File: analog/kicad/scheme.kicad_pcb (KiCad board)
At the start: 2 copper layers, 58 x 24 mm, 17 parts, among them J1 Barrel_Jack_Switch, U1 LM324

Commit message: pcb
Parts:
- added R10: 10k, Resistor_SMD:R_0603_1608Metric, F.Cu at (132.2, 92.0)
- added R11: 12.5k, Resistor_SMD:R_0603_1608Metric, F.Cu at (132.2, 94.5)
- moved R3 3.57 mm to (133.0, 86.0)
- moved R5 0.50 mm to (150.8, 102.0)
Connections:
- net BIAS renamed /BIAS
- J1 pad 1: Net-(U1E-V+) -> Net-(J1-Pad1)
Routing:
- net /BIAS: track 22.5 -> 18.6 mm
- net Net-(J1-Pad1): track 0.00 -> 3.00 mm
- net Net-(U1E-V+): track 49.5 -> 48.2 mm
- net /dist2: track 12.5 -> 11.8 mm

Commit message: changes to pcb
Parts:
- removed the R10 at (132.2, 92.0)
- removed the R11 at (132.2, 94.5)
- added C3: 10u, Capacitor_SMD:C_0805_2012Metric, F.Cu at (128.0, 93.5)
- added C4: 10u, Capacitor_SMD:C_0805_2012Metric, F.Cu at (137.5, 100.5)
- added R7: 1.6k, Resistor_SMD:R_0805_2012Metric, F.Cu at (131.4, 95.0)
- added R8: 4.7k, Resistor_SMD:R_0805_2012Metric, F.Cu at (131.4, 90.8)
- added U2: LM7805_TO220, Package_TO_SOT_THT:TO-220-3_Vertical, F.Cu at (128.4, 101.0)
- C1, C2: footprint Capacitor_SMD:C_0603_1608Metric -> Capacitor_SMD:C_0805_2012Metric
- R1: renamed from R2; footprint Resistor_SMD:R_0603_1608Metric -> Resistor_SMD:R_0805_2012Metric
- R10: renamed from R8; footprint Resistor_SMD:R_0603_1608Metric -> Resistor_SMD:R_0805_2012Metric
- R11: renamed from R9; footprint Resistor_SMD:R_0603_1608Metric -> Resistor_SMD:R_0805_2012Metric
- R2: renamed from R1; footprint Resistor_SMD:R_0603_1608Metric -> Resistor_SMD:R_0805_2012Metric
- R3, R4, R5, R6: footprint Resistor_SMD:R_0603_1608Metric -> Resistor_SMD:R_0805_2012Metric
- R9: renamed from R7; footprint Resistor_SMD:R_0603_1608Metric -> Resistor_SMD:R_0805_2012Metric
- moved J1 4.00 mm to (124.3, 92.0)
- moved R2 0.90 mm to (137.4, 95.2)
- moved R5 0.51 mm to (150.8, 102.5)
- moved C1 0.50 mm to (140.0, 95.3)
- moved R6 0.50 mm to (158.0, 102.5)
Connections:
- net Net-(U1E-V+) renamed +5V
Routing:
- net +5V: track 48.2 -> 72.7 mm
- net Net-(U2-GND): track 0.00 -> 10.4 mm
- net Net-(U2-VI): track 3.00 -> 11.5 mm
- net /BIAS: track 18.6 -> 17.0 mm
- net /OUT: track 30.0 -> 29.2 mm
- net Net-(D1-A): track 16.7 -> 16.1 mm
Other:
- board size 58 x 24 mm -> 62.5 x 27 mm

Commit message: comments and schematic update
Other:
- board text added: "Peale vaadates on trükkplaat üsna kena, aga mõned asjad jäid silma 1) Komponentide nimed R5, R6 ja D4 on kindlasti liiga trükkplaadi ääre lähedal 2) Mõelge kindlasti, kas saate 0603 komponentide jootmisega hakkama 3) Hetkel on trükkplaadi rajad 0.2 mm ehk ac 8 milsi laiad. ise soovitan rajad teha kindlasti 10/10 reeglite järgi, kusjuures toite rajad soovitan teha isegi laiemad, kuni 40 mils. Kuna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"
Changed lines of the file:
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@@
 		(layer "Edge.Cuts")
+	)
+	(gr_text "Peale vaadates on trükkplaat üsna kena, aga mõned asjad jäid silma\n1) Komponentide nimed R5, R6 ja D4 on kindlasti liiga trükkplaadi ääre lähedal\n2) Mõelge kindlasti, kas saate 0603 komponentide jootmisega hakkama\n3) Hetkel on trükkplaadi rajad 0.2 mm ehk ac 8 milsi laiad. ise soovitan rajad teha kindlasti 10/10\nreeglite järgi, kusjuures toite rajad soovitan teha isegi laiemad, kuni 40 mils. \nKuna plaadil ruumi on, siis ega paha ei tee, kui ka muud rajad on laiemad\n4) lisage nn Power good LED (ehk toitesse üks, mis lihtaslt indikeerib, kas toide on olemas või ei)\n5) Soovitan mõelda, et kas trükkplaat läheb ka kusagile korpusesse ja siis teha \ntrükkplaadi väliskuju korpuse järgi\n6) Viade suurus on hetkel 03/06, soovitan vähemalt 05/08 suurust\n7) Võite kaaluda ka valgusdioodide SMD vastu vahetamisele (aga see on teie otsus).\nKui seade läheb nt korpusesse, ehk ongi THT komponent parem).\n8) U1 on ka kindlasti SMD-na saadaval. Kaaluge, kas selle kasutamine võiks anda mingisuguseid eeliseid\n9) Skeemis vististi mainisin, aga U1 tahab kindlasti toitekondensaatorit ning sisend tahab kaitsmist\n10) Paigutuse mõistes mõelge sellele, et kuivõrd D2-D4 võivad hakata mõjutama mõõtetulemusi. Ehk on kasulikum D2-D4\npaigutada nii, et nad saab plaadiga tasapinda panna (hetkel 90 kraadise nurga all)\n11) Ehk on toite osas mõistlik mõelda mingisuguse patarei lahenduse peale (+ siis sisse/väljalülitamiseks\nmingisugune lüliti ka)\n"
+		(at 107.6 127.8 0)
+		(layer "F.Cu")
+		(effects
+			(font
+				(size 1.27 1.27)
+			)
+			(justify left)
+		)
 	)
 	(segment

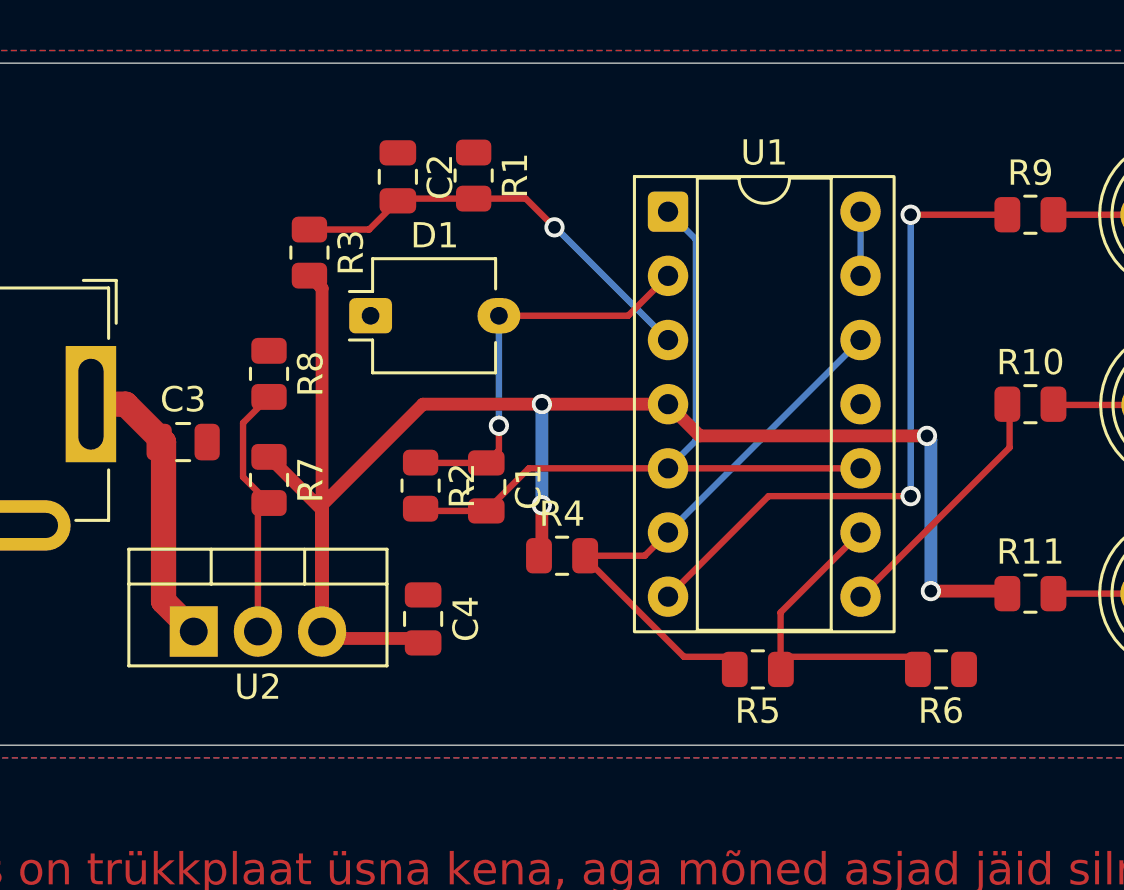
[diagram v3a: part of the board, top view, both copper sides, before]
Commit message: added c5 to pcb
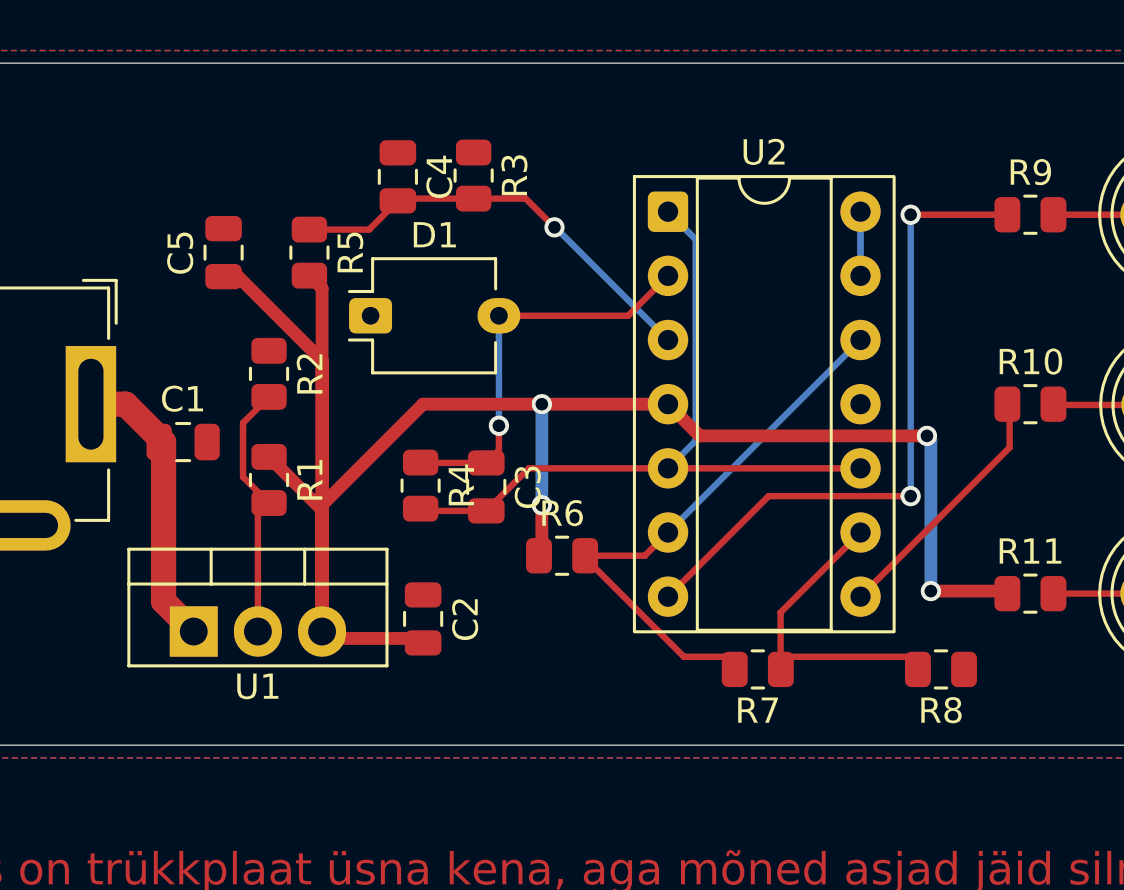
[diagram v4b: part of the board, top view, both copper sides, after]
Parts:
- added C5: 100n, Capacitor_SMD:C_0805_2012Metric, F.Cu at (129.6, 86.0)
- renumbered C3 to C1, C4 to C2, C1 to C3, C2 to C4, R7 to R1, R8 to R2, R1 to R3, R2 to R4, R3 to R5, R4 to R6, R5 to R7, R6 to R8, U2 to U1, U1 to U2
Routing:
- net +5V: track 72.7 -> 88.7 mm

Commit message: pcb cleanup
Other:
- board text removed: "Peale vaadates on trükkplaat üsna kena, aga mõned asjad jäid silma 1) Komponentide nimed R5, R6 ja D4 on kindlasti liiga trükkplaadi ääre lähedal 2) Mõelge kindlasti, kas saate 0603 komponentide jootmisega hakkama 3) Hetkel on trükkplaadi rajad 0.2 mm ehk ac 8 milsi laiad. ise soovitan rajad teha kindlasti 10/10 reeglite järgi, kusjuures toite rajad soovitan teha isegi laiemad, kuni 40 mils. Kuna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"
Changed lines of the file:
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@@
 		(layer "Edge.Cuts")
-	)
-	(gr_text "Peale vaadates on trükkplaat üsna kena, aga mõned asjad jäid silma\n1) Komponentide nimed R5, R6 ja D4 on kindlasti liiga trükkplaadi ääre lähedal\n2) Mõelge kindlasti, kas saate 0603 komponentide jootmisega hakkama\n3) Hetkel on trükkplaadi rajad 0.2 mm ehk ac 8 milsi laiad. ise soovitan rajad teha kindlasti 10/10\nreeglite järgi, kusjuures toite rajad soovitan teha isegi laiemad, kuni 40 mils. \nKuna plaadil ruumi on, siis ega paha ei tee, kui ka muud rajad on laiemad\n4) lisage nn Power good LED (ehk toitesse üks, mis lihtaslt indikeerib, kas toide on olemas või ei)\n5) Soovitan mõelda, et kas trükkplaat läheb ka kusagile korpusesse ja siis teha \ntrükkplaadi väliskuju korpuse järgi\n6) Viade suurus on hetkel 03/06, soovitan vähemalt 05/08 suurust\n7) Võite kaaluda ka valgusdioodide SMD vastu vahetamisele (aga see on teie otsus).\nKui seade läheb nt korpusesse, ehk ongi THT komponent parem).\n8) U1 on ka kindlasti SMD-na saadaval. Kaaluge, kas selle kasutamine võiks anda mingisuguseid eeliseid\n9) Skeemis vististi mainisin, aga U1 tahab kindlasti toitekondensaatorit ning sisend tahab kaitsmist\n10) Paigutuse mõistes mõelge sellele, et kuivõrd D2-D4 võivad hakata mõjutama mõõtetulemusi. Ehk on kasulikum D2-D4\npaigutada nii, et nad saab plaadiga tasapinda panna (hetkel 90 kraadise nurga all)\n11) Ehk on toite osas mõistlik mõelda mingisuguse patarei lahenduse peale (+ siis sisse/väljalülitamiseks\nmingisugune lüliti ka)\n"
-		(at 107.6 127.8 0)
-		(layer "F.Cu")
-		(effects
-			(font
-				(size 1.27 1.27)
-			)
-			(justify left)
-		)
 	)
 	(segment

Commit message: pwr good led
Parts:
- added D5: LED, LED_SMD:LED_0805_2012Metric, F.Cu at (119.6, 82.4)
- added R12: 1k, Resistor_SMD:R_0805_2012Metric, F.Cu at (125.2, 82.4)
- C1: value 10u -> 22p
- C2: value 10u -> 1u
- C3: value 22p -> 10u
- C4: value 1u -> 10u
- R1: value 1.6k -> 220
- R2: value 4.7k -> 500k
- R3: value 220 -> 10k
- R4: value 500k -> 14.7k
- R5: value 10k -> 5k
- R6: value 14.7k -> 10k
- R7: value 5k -> 1.6k
- R8: value 10k -> 4.7k
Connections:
- C1 pad 1: Net-(U1-VI) -> Net-(D1-A)
- C1 pad 2: GND -> /OUT
- C2 pad 1: +5V -> GND
- C2 pad 2: GND -> /BIAS
- C3 pad 1: Net-(D1-A) -> Net-(U1-VI)
- C3 pad 2: /OUT -> GND
- C4 pad 1: GND -> +5V
- C4 pad 2: /BIAS -> GND
- R1 pad 1: +5V -> GND
- R1 pad 2: Net-(U1-GND) -> /BIAS
- R2 pad 1: GND -> Net-(D1-A)
- R2 pad 2: Net-(U1-GND) -> /OUT
- R3 pad 1: GND -> /BIAS
- R3 pad 2: /BIAS -> +5V
- R4 pad 1: Net-(D1-A) -> +5V
- R4 pad 2: /OUT -> /dist3
- R5 pad 1: /BIAS -> /dist2
- R5 pad 2: +5V -> /dist3
- R6 pad 1: +5V -> GND
- R6 pad 2: /dist3 -> /dist2
- R7 pad 1: /dist2 -> +5V
- R7 pad 2: /dist3 -> Net-(U1-GND)
- R8 pad 2: /dist2 -> Net-(U1-GND)
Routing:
- net +5V: track 88.7 -> 94.6 mm
- net Net-(D5-A): track 0.00 -> 5.61 mm

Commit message: fixed pcb
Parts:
- C1: renamed from C3; value 10u -> 22p
- C2: renamed from C4; value 10u -> 1u
- C3: renamed from C1; value 22p -> 10u
- C4: renamed from C2; value 1u -> 10u
- R1: renamed from R3; value 10k -> 220
- R2: renamed from R4; value 14.7k -> 500k
- R3: renamed from R5; value 5k -> 10k
- R4: renamed from R6; value 10k -> 14.7k
- R5: renamed from R7; value 1.6k -> 5k
- R6: renamed from R8; value 4.7k -> 10k
- R7: renamed from R1; value 220 -> 1.6k
- R8: renamed from R2; value 500k -> 4.7k
- moved D5 2.15 mm to (121.6, 83.2)
- moved R12 1.13 mm to (126.0, 83.2)
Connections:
- C1 pad 1: Net-(U1-VI) -> Net-(D1-A)
- C1 pad 2: GND -> /OUT
- C2 pad 1: +5V -> GND
- C2 pad 2: GND -> /BIAS
- C3 pad 1: Net-(D1-A) -> Net-(U1-VI)
- C3 pad 2: /OUT -> GND
- C4 pad 1: GND -> +5V
- C4 pad 2: /BIAS -> GND
- R1 pad 1: /BIAS -> GND
- R1 pad 2: +5V -> /BIAS
- R2 pad 1: +5V -> Net-(D1-A)
- R2 pad 2: /dist3 -> /OUT
- R3 pad 1: /dist2 -> /BIAS
- R3 pad 2: /dist3 -> +5V
- R4 pad 1: GND -> +5V
- R4 pad 2: /dist2 -> /dist3
- R5 pad 1: +5V -> /dist2
- R5 pad 2: Net-(U1-GND) -> /dist3
- R6 pad 2: Net-(U1-GND) -> /dist2
- R7 pad 1: GND -> +5V
- R7 pad 2: /BIAS -> Net-(U1-GND)
- R8 pad 1: Net-(D1-A) -> GND
- R8 pad 2: /OUT -> Net-(U1-GND)
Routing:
- net Net-(D5-A): track 5.61 -> 4.41 mm
- net +5V: track 94.6 -> 93.5 mm
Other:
- board text added: "Peale vaadates on trükkplaat üsna kena, aga mõned asjad jäid silma 1) Komponentide nimed R5, R6 ja D4 on kindlasti liiga trükkplaadi ääre lähedal 2) Mõelge kindlasti, kas saate 0603 komponentide jootmisega hakkama 3) Hetkel on trükkplaadi rajad 0.2 mm ehk ac 8 milsi laiad. ise soovitan rajad teha kindlasti 10/10 reeglite järgi, kusjuures toite rajad soovitan teha isegi laiemad, kuni 40 mils. Kuna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"

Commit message: spacing on pcb
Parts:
- moved R4 1.60 mm to (143.0, 99.6)
- moved R1 1.10 mm to (140.6, 83.0)
- moved C1 0.60 mm to (140.6, 95.3)
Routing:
- net +5V: track 93.5 -> 95.1 mm
- net /dist3: track 22.7 -> 21.8 mm
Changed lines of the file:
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@@
 	(footprint "Resistor_SMD:R_0805_2012Metric"
 		(layer "F.Cu")
-		(at 139.5 82.95 -90)
+		(at 140.6 83 -90)
 		(descr "Resistor SMD 0805 (2012 Metric), square (rectangular) end terminal, IPC-7351 nominal, (Body size source: IPC-SM-782 page 72, https://www.pcb-3d.com/wordpress/wp-content/uploads/ipc-sm-782a_amendment_1_and_2.pdf), generated with kicad-footprint-generator")
 		(tags "resistor")
@@
 	(footprint "Resistor_SMD:R_0805_2012Metric"
 		(layer "F.Cu")
-		(at 143 98)
+		(at 143 99.6)
 		(descr "Resistor SMD 0805 (2012 Metric), square (rectangular) end terminal, IPC-7351 nominal, (Body size source: IPC-SM-782 page 72, https://www.pcb-3d.com/wordpress/wp-content/uploads/ipc-sm-782a_amendment_1_and_2.pdf), generated with kicad-footprint-generator")
 		(tags "resistor")
@@
 	(footprint "Capacitor_SMD:C_0805_2012Metric"
 		(layer "F.Cu")
-		(at 140 95.275 -90)
+		(at 140.6 95.275 -90)
 		(descr "Capacitor SMD 0805 (2012 Metric), square (rectangular) end terminal, IPC-7351 nominal, (Body size source: IPC-SM-782 page 76, https://www.pcb-3d.com/wordpress/wp-content/uploads/ipc-sm-782a_amendment_1_and_2.pdf, https://docs.google.com/spreadsheets/d/1BsfQQcO9C6DZCsRaXUlFlo91Tg2WpOkGARC1WS5S8t0/edit?usp=sharing), generated with kicad-footprint-generator")
 		(tags "capacitor")
@@
 	)
 	(segment
-		(start 139.5 83.8625)
-		(end 141.5625 83.8625)
+		(start 141.6125 83.9125)
+		(end 142.7 85)
 		(width 0.254)
 		(layer "F.Cu")
@@
 	)
 	(segment
-		(start 141.5625 83.8625)
-		(end 142.7 85)
+		(start 136.7 83.95)
+		(end 136.7875 83.8625)
 		(width 0.254)
 		(layer "F.Cu")
@@
 	)
 	(segment
-		(start 136.7 83.95)
-		(end 136.7875 83.8625)
+		(start 140.6 83.9125)
+		(end 141.6125 83.9125)
 		(width 0.254)
 		(layer "F.Cu")
@@
 	)
 	(segment
-		(start 136.7875 83.8625)
-		(end 139.5 83.8625)
+		(start 140.5625 83.95)
+		(end 140.6 83.9125)
 		(width 0.254)
 		(layer "F.Cu")
@@
 		(net 4)
 	)
+	(segment
+		(start 136.5 83.95)
+		(end 140.5625 83.95)
+		(width 0.254)
+		(layer "F.Cu")
+		(net 4)
+	)
 	(via
 		(at 142.7 85)
@@
 	)
 	(segment
-		(start 147.195 97.08)
-		(end 147.32 97.08)
+		(start 147.075 102)
+		(end 150 102)
 		(width 0.254)
 		(layer "F.Cu")
@@
 	)
 	(segment
-		(start 146.275 98)
-		(end 147.195 97.08)
+		(start 143.9125 99.6)
+		(end 144.675 99.6)
 		(width 0.254)
 		(layer "F.Cu")
@@
 	)
 	(segment
-		(start 147.32 97.08)
-		(end 147.5 96.9)
+		(start 147.195 97.08)
+		(end 147.32 97.08)
 		(width 0.254)
 		(layer "F.Cu")
@@
 	)
 	(segment
-		(start 143.825 98)
-		(end 146.275 98)
+		(start 144.675 99.6)
+		(end 147.195 97.08)
 		(width 0.254)
 		(layer "F.Cu")
@@
 	)
 	(segment
-		(start 147.825 102)
-		(end 150 102)
+		(start 147.32 97.08)
+		(end 147.5 96.9)
 		(width 0.254)
 		(layer "F.Cu")
@@
 	)
 	(segment
-		(start 143.825 98)
-		(end 147.825 102)
+		(start 144.675 99.6)
+		(end 147.075 102)
 		(width 0.254)
 		(layer "F.Cu")
@@
 	)
 	(segment
-		(start 142.2 97.975)
-		(end 142.175 98)
-		(width 0.508)
-		(layer "F.Cu")
-		(net 12)
-	)
-	(segment
 		(start 142.2 96)
-		(end 142.2 97.975)
+		(end 142.2 99.4875)
 		(width 0.508)
 		(layer "F.Cu")
@@
 		(width 0.508)
 		(layer "F.Cu")
+		(net 12)
+	)
+	(segment
+		(start 142.2 99.4875)
+		(end 142.0875 99.6)
+		(width 0.508)
+		(layer "F.Cu")
